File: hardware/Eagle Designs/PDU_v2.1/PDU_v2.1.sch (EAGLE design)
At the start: 265 parts, among them J1 5037630291, J10 5037630491, J11 UJ31-CH-G1-SMT-TR, J12 5037630291, J13 5037630291, J14 5037630291, J15 5037630291, J16 5037630291, J17 5037630291, J18 5037630491, J19 5037630291, J2 5037630291, J20 503182-1852, J22 5037630291, J23 5037630291, J24 5037630291, J25 5037630291, J27 5037630691, J3 5037630291, J4 5037630291, J5 5037630291, J6 5037630291, J7 5037630491, J8 5037630491, J9 5037630491, M1 BSZ100N06LS3, M2 BSZ100N06LS3, M3 BSZ033NE2LS5, M4 BSZ033NE2LS5, U1 DRV8847PWPR, U10 AO3404A, U11 IRLML2803PBFCT-ND, U12 IRLML2803PBFCT-ND, U13 LT8390EFE#PBF, U14 ATSAME51N19A-AF, U15 INA219BIDR, U16 MIC2514YM5-TR, U17 MAX16998AAUA+T, U18 TMP36FSZ, U2 DRV8847PWPR, U20 LTC4012IUFPBF, U21 LT8609A, U22 LT8609A, U23 BC848ALT1G, U24 AO3404A, U25 SI4835DDY-T1-GE3, U26 SI3493DDV-T1-GE3, U27 SI3493DDV-T1-GE3, U28 SI4431BDY-T1-E3, U29 AO4818B, U3 LTC1477CS8LINEAR_TECHNOLOGY_L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, U30 INA219BIDR, U31 INA219BIDR, U32 INA219BIDR, U33 INA219BIDR, U4 LTC1477CS8LINEAR_TECHNOLOGY_L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, U5 LTC1477CS8LINEAR_TECHNOLOGY_L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, U6 LTC1477CS8LINEAR_TECHNOLOGY_L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, U7 LTC1477CS8LINEAR_TECHNOLOGY_L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, U8 LT8609A, U9 LTC1477CS8LINEAR_TECHNOLOGY_L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, Y1 ABS07-32.768KHZ-T

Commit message: finalized OBC v4.20; updated PDU v2.1
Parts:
- added C65, C66, C67, C83, C89, C90: 0.1 uF, HSFL_Main_Library:CAP0805
- added R91, R92, R93, R94, R95, R96: (no value), HSFL_Main_Library:RESISTOR0805-RES
- added U19, U34, U35, U36, U37, U38: LND01K1-G, PDU:LND01K1-G
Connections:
- new net N$32: R91.1, U19.DRAIN
- new net N$35: R92.1, U34.DRAIN
- new net N$60: R93.1, U35.DRAIN
- new net N$62: R94.1, U36.DRAIN
- new net N$72: R95.1, U37.DRAIN
- new net N$74: R96.1, U38.DRAIN
- net BUS_3V3: now also C65.1, C66.1
- net BUS_5V: now also C67.1, C83.1, C89.1, C90.1
- net GND: now also C65.2, C66.2, C67.2, C83.2, C89.2, C90.2, R91.2, R92.2, R93.2, R94.2, R95.2, R96.2
- net SW_3V3_1: now also U19.SOURCE
- net SW_3V3_2: now also U34.SOURCE
- net SW_3V3_EN1: now also U19.GATE
- net SW_3V3_EN2: now also U34.GATE
- net SW_5V_1: now also U35.SOURCE
- net SW_5V_2: now also U36.SOURCE
- net SW_5V_3: now also U37.SOURCE
- net SW_5V_4: now also U38.SOURCE
- net SW_5V_EN1: now also U35.GATE
- net SW_5V_EN2: now also U36.GATE
- net SW_5V_EN3: now also U37.GATE
- net SW_5V_EN4: now also U38.GATE
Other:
- note added: "Depletion MOSFETs"
- moved on the sheet: C15, C7, C9, U16, U4, U7

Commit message: updated PDU v2.1 (ongoing board cleanup)
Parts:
- removed R91, R92, R94, R95, R96: (no value), HSFL_Main_Library:RESISTOR0805-RES
- removed U19, U34, U36, U37, U38: LND01K1-G, PDU:LND01K1-G
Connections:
- removed net N$32: R91.1, U19.DRAIN
- removed net N$35: R92.1, U34.DRAIN
- removed net N$62: R94.1, U36.DRAIN
- removed net N$72: R95.1, U37.DRAIN
- removed net N$74: R96.1, U38.DRAIN
- net GND: no longer R91.2, R92.2, R94.2, R95.2, R96.2
- net SD_CS: now also H1.2.49, J20.CD/DAT3; no longer J20.DATA2
- net SD_MISO: now also H1.2.52
- net SD_MOSI: now also H1.2.51
- net SD_SCK: now also H1.2.50
- net SW_3V3_1: no longer U19.SOURCE
- net SW_3V3_2: no longer U34.SOURCE
- net SW_3V3_EN1: no longer U19.GATE
- net SW_3V3_EN2: no longer U34.GATE
- net SW_5V_2: no longer U36.SOURCE
- net SW_5V_3: no longer U37.SOURCE
- net SW_5V_4: no longer U38.SOURCE
- net SW_5V_EN2: no longer U36.GATE
- net SW_5V_EN3: no longer U37.GATE
- net SW_5V_EN4: no longer U38.GATE
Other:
- moved on the sheet: C7, R93, U16, U35

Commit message: completed PDU v2.1 (awaiting feedback)
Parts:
- renumbered C_DC to C91, LED1 to D13, R_CL to R91, R_F to R96, R_IN1 to R92, R_IN2 to R94, R_SENSE to R95
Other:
- note added: "(RIN1)"
- note added: "(RIN2)"
- note added: "(RSENSE)"
- note added: "LED (BATT CHRG)"
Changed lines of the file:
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@@
 <part name="R54" library="HSFL_Main_Library" deviceset="RESISTOR" device="0805-RES" value="3.3 k"/>
 <part name="U20" library="charging" deviceset="LTC4012IUFPBF" device=""/>
-<part name="C_DC" library="HSFL_Main_Library" deviceset="CAP" device="0805" value="0.1 uF"/>
+<part name="C91" library="HSFL_Main_Library" deviceset="CAP" device="0805" value="0.1 uF"/>
 <part name="R27" library="HSFL_Main_Library" deviceset="RESISTOR" device="0805-RES" value="3 k"/>
-<part name="LED1" library="HSFL_Main_Library" deviceset="LED_0805" device=""/>
+<part name="D13" library="HSFL_Main_Library" deviceset="LED_0805" device=""/>
 <part name="U28" library="charging" deviceset="SI4431BDY-T1-E3" device=""/>
 <part name="C10" library="HSFL_Main_Library" deviceset="CAP" device="0805" value="0.1 uF"/>
 <part name="R28" library="HSFL_Main_Library" deviceset="RESISTOR" device="0805-RES" value="6.04 k"/>
 <part name="C12" library="HSFL_Main_Library" deviceset="CAP" device="0805" value="0.1 uF"/>
-<part name="R_F" library="HSFL_Main_Library" deviceset="RESISTOR" device="0805-RES" value="5.1 k"/>
-<part name="R_CL" library="HSFL_Main_Library" deviceset="RESISTOR" device="0805-RES" value="1"/>
+<part name="R96" library="HSFL_Main_Library" deviceset="RESISTOR" device="0805-RES" value="5.1 k"/>
+<part name="R91" library="HSFL_Main_Library" deviceset="RESISTOR" device="0805-RES" value="1"/>
 <part name="C14" library="HSFL_Main_Library" deviceset="CAP" device="0805" value="10 uF"/>
 <part name="R29" library="HSFL_Main_Library" deviceset="RESISTOR" device="0805-RES" value="0"/>
@@
 <part name="C18" library="HSFL_Main_Library" deviceset="CAP" device="0805" value="0.1 uF"/>
 <part name="L2" library="charging" deviceset="AIML-0805-150K-T" device=""/>
-<part name="R_IN1" library="HSFL_Main_Library" deviceset="RESISTOR" device="0805-RES" value="3.01 k"/>
-<part name="R_IN2" library="HSFL_Main_Library" deviceset="RESISTOR" device="0805-RES" value="3.01 k"/>
-<part name="R_SENSE" library="HSFL_Main_Library" deviceset="RESISTOR" device="0805-RES" value="1"/>
+<part name="R92" library="HSFL_Main_Library" deviceset="RESISTOR" device="0805-RES" value="3.01 k"/>
+<part name="R94" library="HSFL_Main_Library" deviceset="RESISTOR" device="0805-RES" value="3.01 k"/>
+<part name="R95" library="HSFL_Main_Library" deviceset="RESISTOR" device="0805-RES" value="1"/>
 <part name="C38" library="HSFL_Main_Library" deviceset="CAP" device="0805" value="4.7 uF"/>
 <part name="R37" library="HSFL_Main_Library" deviceset="RESISTOR" device="0805-RES" value="26.7 k"/>
@@
 <text x="-71.12" y="78.74" size="1.27" layer="97">~ICL left floating
 when unused (pg. 8)</text>
+<text x="7.62" y="33.02" size="1.778" layer="97">(RIN1)</text>
+<text x="7.62" y="22.86" size="1.778" layer="97">(RIN2)</text>
+<text x="30.48" y="25.4" size="1.778" layer="97">(RSENSE)</text>
+<text x="-60.96" y="129.54" size="1.778" layer="97">LED (BATT CHRG)</text>
 </plain>
 <instances>
@@
 <attribute name="VALUE" x="-45.0342" y="-8.3566" size="2.0828" layer="96" ratio="10" rot="SR0"/>
 </instance>
-<instance part="C_DC" gate="G$1" x="-81.28" y="137.16" smashed="yes">
+<instance part="C91" gate="G$1" x="-81.28" y="137.16" smashed="yes">
 <attribute name="NAME" x="-79.756" y="140.081" size="1.778" layer="95"/>
 <attribute name="VALUE" x="-79.756" y="135.001" size="1.778" layer="96"/>
@@
 <attribute name="VALUE" x="-62.23" y="133.858" size="1.778" layer="96"/>
 </instance>
-<instance part="LED1" gate="G$1" x="-63.5" y="124.46" smashed="yes">
+<instance part="D13" gate="G$1" x="-63.5" y="124.46" smashed="yes">
 <attribute name="NAME" x="-60.96" y="127" size="1.778" layer="95"/>
 </instance>
@@
 <attribute name="VALUE" x="4.064" y="112.141" size="1.778" layer="96"/>
 </instance>
-<instance part="R_F" gate="G$1" x="20.32" y="111.76" smashed="yes">
+<instance part="R96" gate="G$1" x="20.32" y="111.76" smashed="yes">
 <attribute name="NAME" x="16.51" y="113.2586" size="1.778" layer="95"/>
 <attribute name="VALUE" x="16.51" y="108.458" size="1.778" layer="96"/>
 </instance>
-<instance part="R_CL" gate="G$1" x="7.62" y="124.46" smashed="yes">
+<instance part="R91" gate="G$1" x="7.62" y="124.46" smashed="yes">
 <attribute name="NAME" x="11.43" y="125.9586" size="1.778" layer="95"/>
 <attribute name="VALUE" x="11.43" y="121.158" size="1.778" layer="96"/>
@@
 <attribute name="NAME" x="49.8856" y="74.4728" size="1.778" layer="95" ratio="10" rot="SR0"/>
 </instance>
-<instance part="R_IN1" gate="G$1" x="2.54" y="33.02" smashed="yes">
+<instance part="R92" gate="G$1" x="2.54" y="33.02" smashed="yes">
 <attribute name="NAME" x="-1.27" y="34.5186" size="1.778" layer="95"/>
 <attribute name="VALUE" x="-1.27" y="29.718" size="1.778" layer="96"/>
 </instance>
-<instance part="R_IN2" gate="G$1" x="2.54" y="22.86" smashed="yes">
+<instance part="R94" gate="G$1" x="2.54" y="22.86" smashed="yes">
 <attribute name="NAME" x="-1.27" y="24.3586" size="1.778" layer="95"/>
 <attribute name="VALUE" x="-1.27" y="19.558" size="1.778" layer="96"/>
 </instance>
-<instance part="R_SENSE" gate="G$1" x="22.86" y="27.94" smashed="yes" rot="R90">
+<instance part="R95" gate="G$1" x="22.86" y="27.94" smashed="yes" rot="R90">
 <attribute name="NAME" x="24.13" y="26.8986" size="1.778" layer="95"/>
 <attribute name="VALUE" x="24.13" y="24.638" size="1.778" layer="96"/>
@@
 </segment>
 <segment>
-<pinref part="C_DC" gate="G$1" pin="2"/>
+<pinref part="C91" gate="G$1" pin="2"/>
 <wire x1="-81.28" y1="134.62" x2="-81.28" y2="132.08" width="0.1524" layer="91"/>
 <label x="-83.82" y="129.54" size="1.778" layer="95"/>
@@
 <wire x1="-63.5" y1="142.24" x2="-63.5" y2="144.78" width="0.1524" layer="91"/>
 <wire x1="-63.5" y1="144.78" x2="-71.12" y2="144.78" width="0.1524" layer="91"/>
-<pinref part="C_DC" gate="G$1" pin="1"/>
+<pinref part="C91" gate="G$1" pin="1"/>
 <wire x1="-71.12" y1="144.78" x2="-81.28" y2="144.78" width="0.1524" layer="91"/>
 <wire x1="-81.28" y1="144.78" x2="-93.98" y2="144.78" width="0.1524" layer="91"/>
@@
 <pinref part="U20" gate="A" pin="~CHRG"/>
 <wire x1="-53.34" y1="119.38" x2="-63.5" y2="119.38" width="0.1524" layer="91"/>
-<pinref part="LED1" gate="G$1" pin="2"/>
+<pinref part="D13" gate="G$1" pin="2"/>
 <wire x1="-63.5" y1="124.46" x2="-63.5" y2="119.38" width="0.1524" layer="91"/>
 <label x="-60.96" y="119.38" size="1.778" layer="95"/>
@@
 <segment>
 <pinref part="R27" gate="G$1" pin="1"/>
-<pinref part="LED1" gate="G$1" pin="1"/>
+<pinref part="D13" gate="G$1" pin="1"/>
 <wire x1="-63.5" y1="132.08" x2="-63.5" y2="129.54" width="0.1524" layer="91"/>
 </segment>
@@
 <junction x="-7.62" y="111.76"/>
 <label x="-15.24" y="111.76" size="1.778" layer="95"/>
-<pinref part="R_CL" gate="G$1" pin="1"/>
+<pinref part="R91" gate="G$1" pin="1"/>
 <wire x1="2.54" y1="124.46" x2="-7.62" y2="124.46" width="0.1524" layer="91"/>
 </segment>
@@
 <wire x1="10.16" y1="111.76" x2="15.24" y2="111.76" width="0.1524" layer="91"/>
 <junction x="10.16" y="111.76"/>
-<pinref part="R_F" gate="G$1" pin="1"/>
+<pinref part="R96" gate="G$1" pin="1"/>
 </segment>
 </net>
@@
 </segment>
 <segment>
-<pinref part="R_IN1" gate="G$1" pin="2"/>
-<pinref part="R_SENSE" gate="G$1" pin="2"/>
+<pinref part="R92" gate="G$1" pin="2"/>
+<pinref part="R95" gate="G$1" pin="2"/>
 <wire x1="7.62" y1="33.02" x2="22.86" y2="33.02" width="0.1524" layer="91"/>
 <wire x1="22.86" y1="33.02" x2="27.94" y2="33.02" width="0.1524" layer="91"/>
@@
 <pinref part="U20" gate="A" pin="CSP"/>
 <wire x1="-15.24" y1="33.02" x2="-2.54" y2="33.02" width="0.1524" layer="91"/>
-<pinref part="R_IN1" gate="G$1" pin="1"/>
+<pinref part="R92" gate="G$1" pin="1"/>
 </segment>
 </net>
@@
 <pinref part="U20" gate="A" pin="CSN"/>
 <wire x1="-15.24" y1="22.86" x2="-2.54" y2="22.86" width="0.1524" layer="91"/>
-<pinref part="R_IN2" gate="G$1" pin="1"/>
+<pinref part="R94" gate="G$1" pin="1"/>
 </segment>
 </net>
@@
 <net name="VBATT" class="0">
 <segment>
-<pinref part="R_CL" gate="G$1" pin="2"/>
+<pinref part="R91" gate="G$1" pin="2"/>
 <pinref part="C14" gate="G$1" pin="1"/>
 <wire x1="12.7" y1="124.46" x2="30.48" y2="124.46" width="0.1524" layer="91"/>
 <wire x1="30.48" y1="124.46" x2="30.48" y2="111.76" width="0.1524" layer="91"/>
-<pinref part="R_F" gate="G$1" pin="2"/>
+<pinref part="R96" gate="G$1" pin="2"/>
 <wire x1="30.48" y1="111.76" x2="30.48" y2="109.22" width="0.1524" layer="91"/>
 <wire x1="25.4" y1="111.76" x2="30.48" y2="111.76" width="0.1524" layer="91"/>
@@
 <segment>
 <pinref part="U20" gate="A" pin="BAT"/>
-<pinref part="R_SENSE" gate="G$1" pin="1"/>
+<pinref part="R95" gate="G$1" pin="1"/>
 <wire x1="-15.24" y1="15.24" x2="22.86" y2="15.24" width="0.1524" layer="91"/>
 <wire x1="22.86" y1="15.24" x2="22.86" y2="22.86" width="0.1524" layer="91"/>
@@
 <wire x1="22.86" y1="15.24" x2="33.02" y2="15.24" width="0.1524" layer="91"/>
 <junction x="22.86" y="15.24"/>
-<pinref part="R_IN2" gate="G$1" pin="2"/>
+<pinref part="R94" gate="G$1" pin="2"/>
 <wire x1="7.62" y1="22.86" x2="22.86" y2="22.86" width="0.1524" layer="91"/>
 <junction x="22.86" y="22.86"/>

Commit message: finalized PDU v2.1 and generated Gerber Files
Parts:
- added C92: 1 uF, HSFL_Main_Library:CAP1206
- added R97: 16, HSFL_Main_Library:RESISTOR0805-RES
- C44: value 1uF -> 1 uF
- R93: value (none) -> 10 k
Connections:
- new net POST_RBF_VBATT: R97.1, U24.S
- net CS_VBATT: now also C92.1, R97.2; no longer U24.S
- net GND: now also C92.2
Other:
- note added: "PY_VBATT: Power source directly from PyCubed Battery Board (Pre-RBF Circuit) POST_RBF_VBATT: Power source that gets (noise) filtered (Post-RBF Circuit)"
- note removed: "PY_VBATT: Power source directly from PyCubed Battery Board (Pre-RBF Circuit) CS_VBATT: Power source that supplies to Current Sensor (Post-RBF Circuit)"
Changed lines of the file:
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@@
 <part name="GND51" library="SparkFun-PowerSymbols" library_urn="urn:adsk.eagle:library:530" deviceset="GND" device=""/>
 <part name="C43" library="HSFL_Main_Library" deviceset="CAP" device="0805" value="4.7 uF"/>
-<part name="C44" library="HSFL_Main_Library" deviceset="CAP" device="0805" value="1uF"/>
+<part name="C44" library="HSFL_Main_Library" deviceset="CAP" device="0805" value="1 uF"/>
 <part name="C45" library="HSFL_Main_Library" deviceset="CAP" device="0805" value="0.1 uF"/>
 <part name="R6" library="HSFL_Main_Library" deviceset="RESISTOR" device="0805-RES" value="100 k"/>
@@
 <part name="C90" library="HSFL_Main_Library" deviceset="CAP" device="0805" value="0.1 uF"/>
 <part name="U35" library="PDU" deviceset="LND01K1-G" device=""/>
-<part name="R93" library="HSFL_Main_Library" deviceset="RESISTOR" device="0805-RES"/>
+<part name="R93" library="HSFL_Main_Library" deviceset="RESISTOR" device="0805-RES" value="10 k"/>
+<part name="C92" library="HSFL_Main_Library" deviceset="CAP" device="1206" value="1 uF"/>
+<part name="R97" library="HSFL_Main_Library" deviceset="RESISTOR" device="0805-RES" value="16"/>
 </parts>
 <sheets>
@@
 </sheet>
 <sheet>
+<description>Low Pass Filter / RC Circuit</description>
+<plain>
+<text x="27.94" y="15.24" size="1.27" layer="97" rot="R180">0805</text>
+<text x="38.1" y="2.54" size="1.27" layer="97" rot="R180">1206</text>
+</plain>
+<instances>
+<instance part="C92" gate="G$1" x="33.02" y="5.08" smashed="yes">
+<attribute name="NAME" x="34.544" y="8.001" size="1.778" layer="95"/>
+<attribute name="VALUE" x="34.544" y="2.921" size="1.778" layer="96"/>
+</instance>
+<instance part="R97" gate="G$1" x="22.86" y="12.7" smashed="yes">
+<attribute name="NAME" x="19.05" y="14.1986" size="1.778" layer="95"/>
+<attribute name="VALUE" x="19.05" y="9.398" size="1.778" layer="96"/>
+</instance>
+</instances>
+<busses>
+</busses>
+<nets>
+<net name="POST_RBF_VBATT" class="0">
+<segment>
+<wire x1="17.78" y1="12.7" x2="7.62" y2="12.7" width="0.1524" layer="91"/>
+<label x="-12.7" y="12.7" size="1.778" layer="95"/>
+<pinref part="R97" gate="G$1" pin="1"/>
+</segment>
+</net>
+<net name="CS_VBATT" class="0">
+<segment>
+<wire x1="27.94" y1="12.7" x2="33.02" y2="12.7" width="0.1524" layer="91"/>
+<label x="40.64" y="12.7" size="1.778" layer="95"/>
+<wire x1="33.02" y1="12.7" x2="40.64" y2="12.7" width="0.1524" layer="91"/>
+<wire x1="33.02" y1="12.7" x2="33.02" y2="10.16" width="0.1524" layer="91"/>
+<junction x="33.02" y="12.7"/>
+<pinref part="C92" gate="G$1" pin="1"/>
+<pinref part="R97" gate="G$1" pin="2"/>
+</segment>
+</net>
+<net name="GND" class="0">
+<segment>
+<wire x1="33.02" y1="2.54" x2="33.02" y2="0" width="0.1524" layer="91"/>
+<label x="30.48" y="-2.54" size="1.778" layer="95"/>
+<wire x1="33.02" y1="0" x2="7.62" y2="0" width="0.1524" layer="91"/>
+<wire x1="33.02" y1="0" x2="40.64" y2="0" width="0.1524" layer="91"/>
+<junction x="33.02" y="0"/>
+<pinref part="C92" gate="G$1" pin="2"/>
+</segment>
+</net>
+</nets>
+</sheet>
+<sheet>
 <description>H-Bridge Circuits</description>
 <plain>
@@
 <instance part="R93" gate="G$1" x="124.46" y="-139.7" smashed="yes">
 <attribute name="NAME" x="120.65" y="-143.2814" size="1.778" layer="95"/>
-<attribute name="VALUE" x="120.65" y="-143.002" size="1.778" layer="96"/>
+<attribute name="VALUE" x="120.65" y="-145.542" size="1.778" layer="96"/>
 </instance>
 </instances>
@@
 <text x="99.06" y="-38.1" size="1.778" layer="97">PY_VBATT: Power source directly from PyCubed Battery Board
 (Pre-RBF Circuit)
-CS_VBATT: Power source that supplies to Current Sensor (Post-RBF Circuit)</text>
+POST_RBF_VBATT: Power source that gets (noise) filtered (Post-RBF Circuit)</text>
 <text x="10.16" y="-43.18" size="1.778" layer="97">Male Connector (MC) External Part Not Shown
 MC in (Pin In)
@@
 </segment>
 </net>
-<net name="CS_VBATT" class="0">
+<net name="POST_RBF_VBATT" class="0">
 <segment>
 <pinref part="U24" gate="A" pin="S"/>
 <wire x1="86.36" y1="-10.16" x2="81.28" y2="-10.16" width="0.1524" layer="91"/>
 <wire x1="81.28" y1="-10.16" x2="81.28" y2="-15.24" width="0.1524" layer="91"/>
-<label x="76.2" y="-17.78" size="1.778" layer="95"/>
+<label x="71.12" y="-17.78" size="1.778" layer="95"/>
 </segment>
 </net>

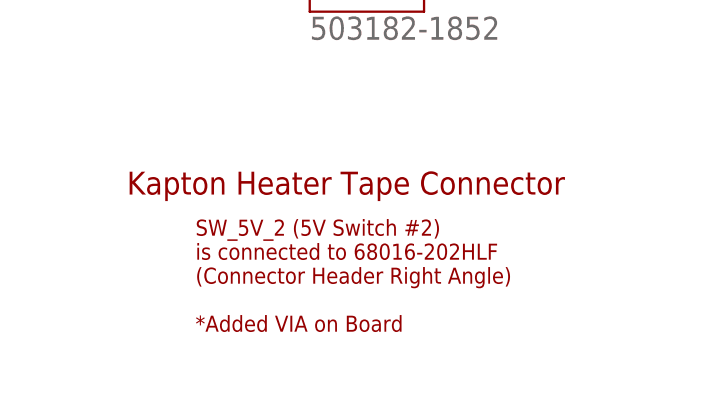
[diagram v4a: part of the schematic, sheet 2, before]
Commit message: added Kapton Heater Connector (device) to PDU v2.1
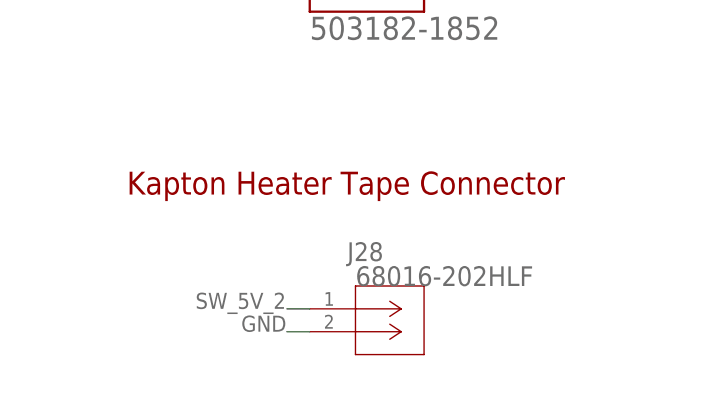
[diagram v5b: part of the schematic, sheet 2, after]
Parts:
- added J28: 68016-202HLF, PDU:68016-202HLF
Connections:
- net GND: now also J28.2
- net SW_5V_2: now also J28.1
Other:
- note removed: "SW_5V_2 (5V Switch #2) is connected to 68016-202HLF (Connector Header Right Angle) *Added VIA on Board"
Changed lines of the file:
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@@
 <part name="C92" library="HSFL_Main_Library" deviceset="CAP" device="1206" value="1 uF"/>
 <part name="R97" library="HSFL_Main_Library" deviceset="RESISTOR" device="0805-RES" value="16"/>
+<part name="J28" library="PDU" deviceset="68016-202HLF" device=""/>
 </parts>
 <sheets>
@@
 <text x="127" y="99.06" size="1.778" layer="97">0603</text>
 <text x="127" y="96.52" size="1.778" layer="97">0603</text>
-<text x="142.24" y="-17.78" size="1.778" layer="94">SW_5V_2 (5V Switch #2)
-is connected to 68016-202HLF
-(Connector Header Right Angle)
-*Added VIA on Board</text>
 <text x="-17.78" y="40.64" size="1.27" layer="97">PY_VBATT is used for
 Pre-RBF Circuit.</text>
@@
 <attribute name="VALUE" x="91.44" y="60.96" size="2.1844" layer="96"/>
 <attribute name="NAME" x="91.44" y="63.5" size="2.1844" layer="95"/>
+</instance>
+<instance part="J28" gate="G$1" x="160.02" y="-20.32" smashed="yes">
+<attribute name="NAME" x="159.1056" y="-9.9314" size="2.0828" layer="95" ratio="6" rot="SR0"/>
+<attribute name="VALUE" x="160.02" y="-12.7" size="2.1844" layer="96"/>
 </instance>
 </instances>
@@
 <label x="76.2" y="48.26" size="1.778" layer="95"/>
 </segment>
+<segment>
+<pinref part="J28" gate="G$1" pin="2"/>
+<wire x1="154.94" y1="-17.78" x2="152.4" y2="-17.78" width="0.1524" layer="91"/>
+<label x="147.32" y="-17.78" size="1.778" layer="95"/>
+</segment>
 </net>
 <net name="SOLAR_IN5" class="0">
@@
 </segment>
 </net>
+<net name="SW_5V_2" class="0">
+<segment>
+<pinref part="J28" gate="G$1" pin="1"/>
+<wire x1="154.94" y1="-15.24" x2="152.4" y2="-15.24" width="0.1524" layer="91"/>
+<label x="142.24" y="-15.24" size="1.778" layer="95"/>
+</segment>
+</net>
